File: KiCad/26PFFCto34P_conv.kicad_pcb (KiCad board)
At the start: 2 copper layers, 48 x 18 mm, 9 parts, among them J1 Conn_02x17_Odd_Even, J2 Ready, J3 DSx, J4 2HD, J5 -+, J6 FD_FFC_26p

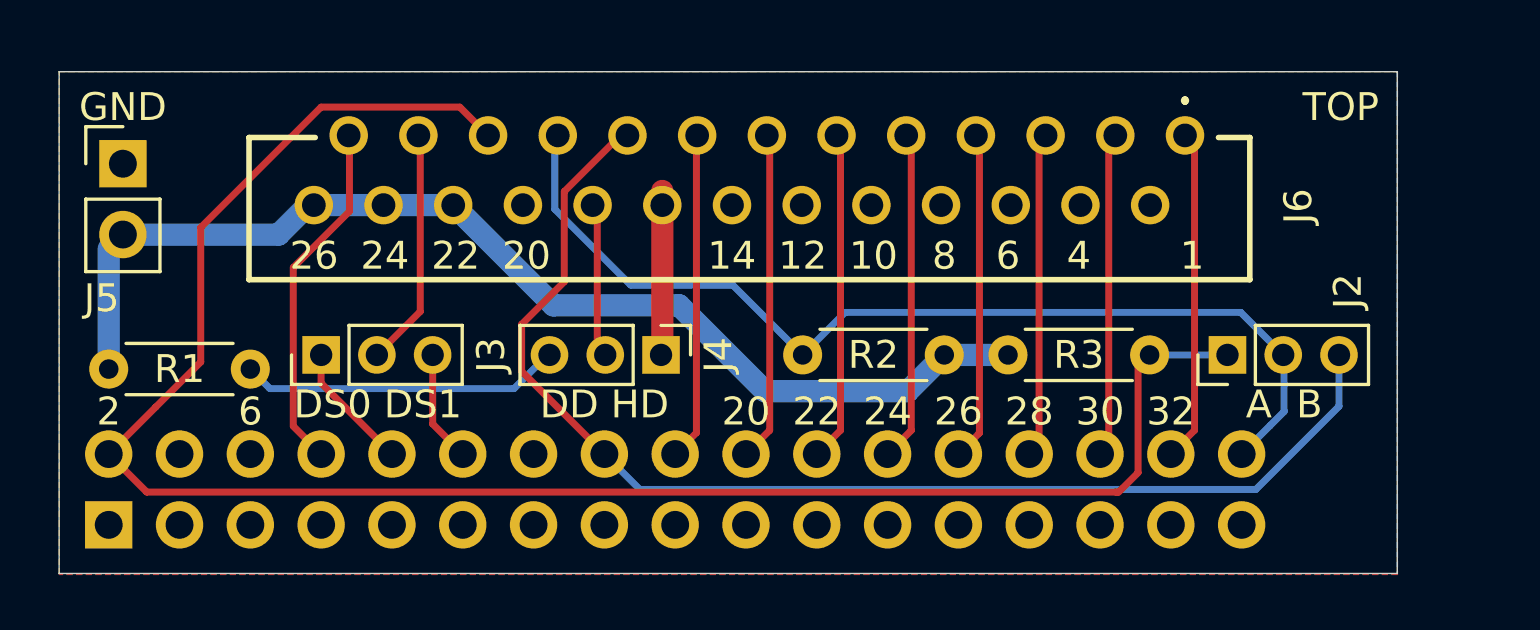
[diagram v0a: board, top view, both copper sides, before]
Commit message: DS1 fixed. width 48mm to 50mm
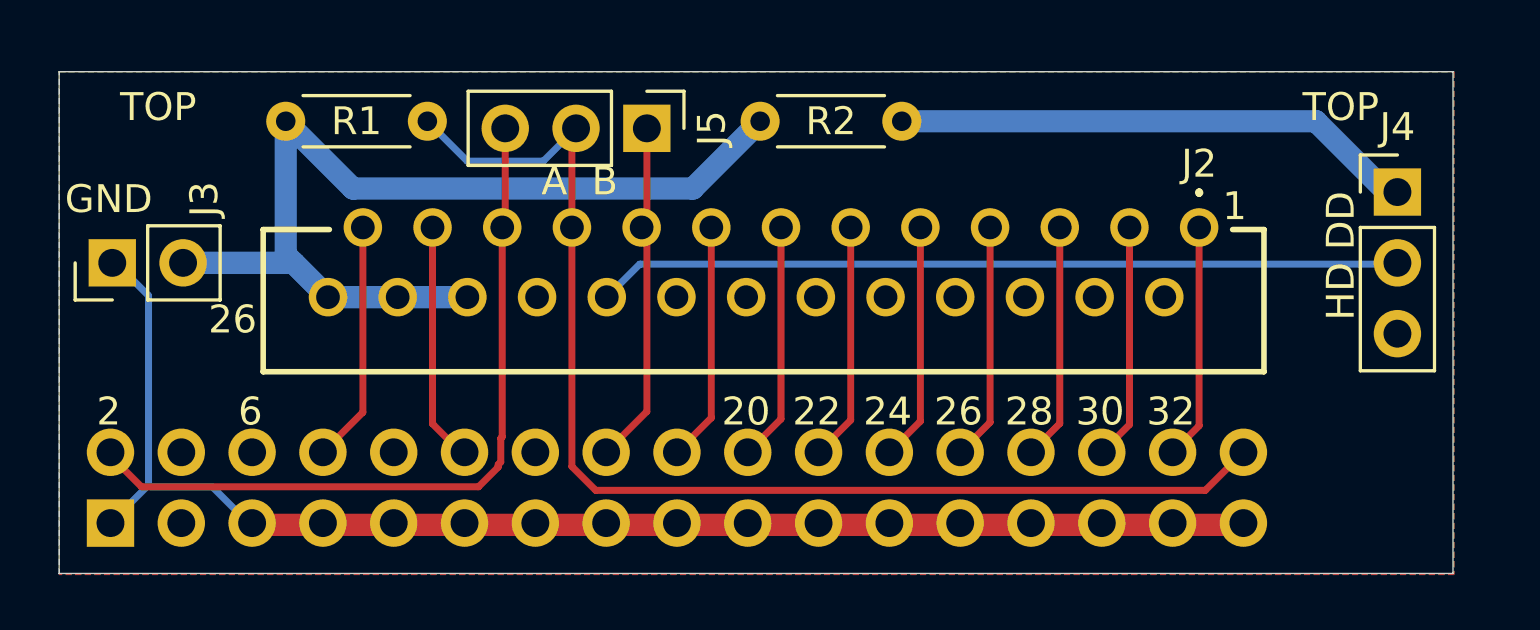
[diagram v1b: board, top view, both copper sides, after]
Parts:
- removed J6: FD_FFC_26p, kicad_by_BakudaLab:520452645
- removed R3: 4.7K, Resistor_THT:R_Axial_DIN0204_L3.6mm_D1.6mm_P5.08mm_Horizontal
- J1: value Conn_02x17_Odd_Even -> FDD
- J2: value Ready -> FDC; footprint Connector_PinHeader_2.00mm:PinHeader_1x03_P2.00mm_Vertical -> kicad_by_BakudaLab:morex520452645
- J3: value DSx -> -+; footprint Connector_PinHeader_2.00mm:PinHeader_1x03_P2.00mm_Vertical -> Connector_PinHeader_2.54mm:PinHeader_1x02_P2.54mm_Vertical
- J4: value 2HD -> Conn_01x03; footprint Connector_PinHeader_2.00mm:PinHeader_1x03_P2.00mm_Vertical -> Connector_PinHeader_2.54mm:PinHeader_1x03_P2.54mm_Vertical
- J5: value -+ -> Conn_01x03; footprint Connector_PinHeader_2.54mm:PinHeader_1x02_P2.54mm_Vertical -> Connector_PinHeader_2.54mm:PinHeader_1x03_P2.54mm_Vertical
- moved J4 27.1 mm to (98.8, 55.1), turned to 0 degrees
- moved J5 18.8 mm to (71.9, 52.8), turned to 270 degrees
- moved R1 10.9 mm to (58.9, 52.6)
- moved R2 10.7 mm to (75.9, 52.6), turned to 0 degrees
- moved J3 8.19 mm to (52.7, 57.7)
- moved J2 4.68 mm to (91.7, 56.4), turned to 180 degrees
- moved J1 0.09 mm to (52.6, 67.0)
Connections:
- J1 pad 10: /DS0# -> Net-(J1-Pad10)
- J1 pad 3: GND -> Net-(J1-Pad3)
- J2 pad 1: /DISKCHANGE# -> /SIDE1
- J2 pad 2: /READY# -> GND
- J2 pad 3: /MOTORON# -> /READDATA#
- J3 pad 1: /DS0# -> GND
- J3 pad 2: Net-(J3-Pad2) -> +5V
- J4 pad 1: GND -> Net-(J4-Pad1)
- J4 pad 2: Net-(J4-Pad2) -> /HDOUT#
- J4 pad 3: Net-(J4-Pad3) -> GND
- J5 pad 1: GND -> /MOTORON#
- J5 pad 2: +5V -> /READY#
- R1 pad 2: Net-(J4-Pad3) -> /READY#
- R2 pad 2: /READY# -> Net-(J4-Pad1)
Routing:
- net GND: track 5.67 -> 50.9 mm
- net /DISKCHANGE#: track 66.6 -> 27.0 mm
- net /MOTORON#: track 44.3 -> 12.6 mm
- net /HDOUT#: track 0.00 -> 28.9 mm
- net Net-(J4-Pad1): track 0.00 -> 18.8 mm
- net Net-(J4-Pad3): track 11.5 -> 0.00 mm
- net Net-(J3-Pad2): track 8.52 -> 0.00 mm
- net /READY#: track 36.4 -> 43.6 mm
- net Net-(J4-Pad2): track 5.33 -> 0.00 mm
- net /DS0#: track 4.61 -> 0.00 mm
- net /DS1#: track 4.00 -> 8.58 mm
- net /INDEX#: track 12.7 -> 8.75 mm
- net /WRITEGATE#: track 12.4 -> 8.62 mm
- net /STEP#: track 11.8 -> 8.65 mm
- net /DIR#: track 11.7 -> 8.66 mm
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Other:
- board size 48 x 18 mm -> 50 x 18 mm
- board text added: "FFC 26P to 34P Version 0.1 by Bakuda Lab 2021"
- board text added: "HD DD"
- board text removed: "10"
- board text removed: "12"
- board text removed: "14"
- board text removed: "4"
- board text removed: "8"
- board text removed: "DD HD"
- board text removed: "DS0 DS1"
- board text removed: "FFC 26P to 34P Ver.0 by Bakuda Lab 2021"

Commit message: Further miniaturization
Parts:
- J2: footprint kicad_by_BakudaLab:morex520452645 -> 26PFFCto34P_conv:morex520452645
- moved J4 15.2 mm to (83.8, 52.7), turned to 90 degrees
- moved J3 1.40 mm to (52.7, 59.1)
- moved J1 1.14 mm to (52.6, 65.8)
- moved R1 0.27 mm to (58.9, 52.8)
- moved J2 0.25 mm to (91.7, 56.6)
- moved J5 0.13 mm to (71.9, 52.7)
- moved R2 0.13 mm to (75.9, 52.7)
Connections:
- net /DIR# renamed /DIR
- net /DISKCHANGE# renamed /DISKCHANGE
- net /DS1# renamed /DRIVESELECT
- net /INDEX# renamed /INDEX
- net /READDATA# renamed /READDATA
- net /READY# renamed /READY
- net /STEP# renamed /STEP
- net /TRACK00# renamed /TRACK00
- net /WRITEDATA# renamed /WRITEDATA
- net /WRITEGATE# renamed /WRITEGATE
- net /WRITEPROTECT# renamed /WRITEPROTECT
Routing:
- net GND: track 50.9 -> 13.8 mm
- net Net-(J4-Pad1): track 18.8 -> 2.79 mm
- net /HDOUT#: track 28.9 -> 19.1 mm
- net /DRIVESELECT: track 8.58 -> 7.14 mm
- net /READY: track 43.6 -> 42.2 mm
- net /WRITEPROTECT: track 8.58 -> 7.18 mm
- net /WRITEGATE: track 8.62 -> 7.22 mm
- net /WRITEDATA: track 8.63 -> 7.23 mm
- net /READDATA: track 8.57 -> 7.17 mm
- net /INDEX: track 8.75 -> 7.35 mm
- net /TRACK00: track 8.60 -> 7.20 mm
- net /STEP: track 8.65 -> 7.25 mm
- net /SIDE1: track 8.55 -> 7.15 mm
- net /DIR: track 8.66 -> 7.27 mm
- net /MOTORON#: track 12.6 -> 11.3 mm
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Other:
- board size 50 x 18 mm -> 50 x 17 mm
- board text added: "-A--B-"
- board text added: "-DD-HD-"
- board text added: "0"
- board text added: "25"
- board text added: "26P FFC to 34P Shugart Version 0.1 by Bakuda Lab 2021"
- board text added: "34"
- board text added: "VL1/VL1m/VL7"
- board text removed: "20"
- board text removed: "22"
- board text removed: "24"
- board text removed: "26"
- board text removed: "28"
- board text removed: "30"
- board text removed: "32"
- board text removed: "A B"
- board text removed: "FFC 26P to 34P Version 0.1 by Bakuda Lab 2021"
- board text removed: "HD DD"
